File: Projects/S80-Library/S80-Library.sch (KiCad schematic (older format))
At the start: 2 parts, among them U1 ATmega328P-PU

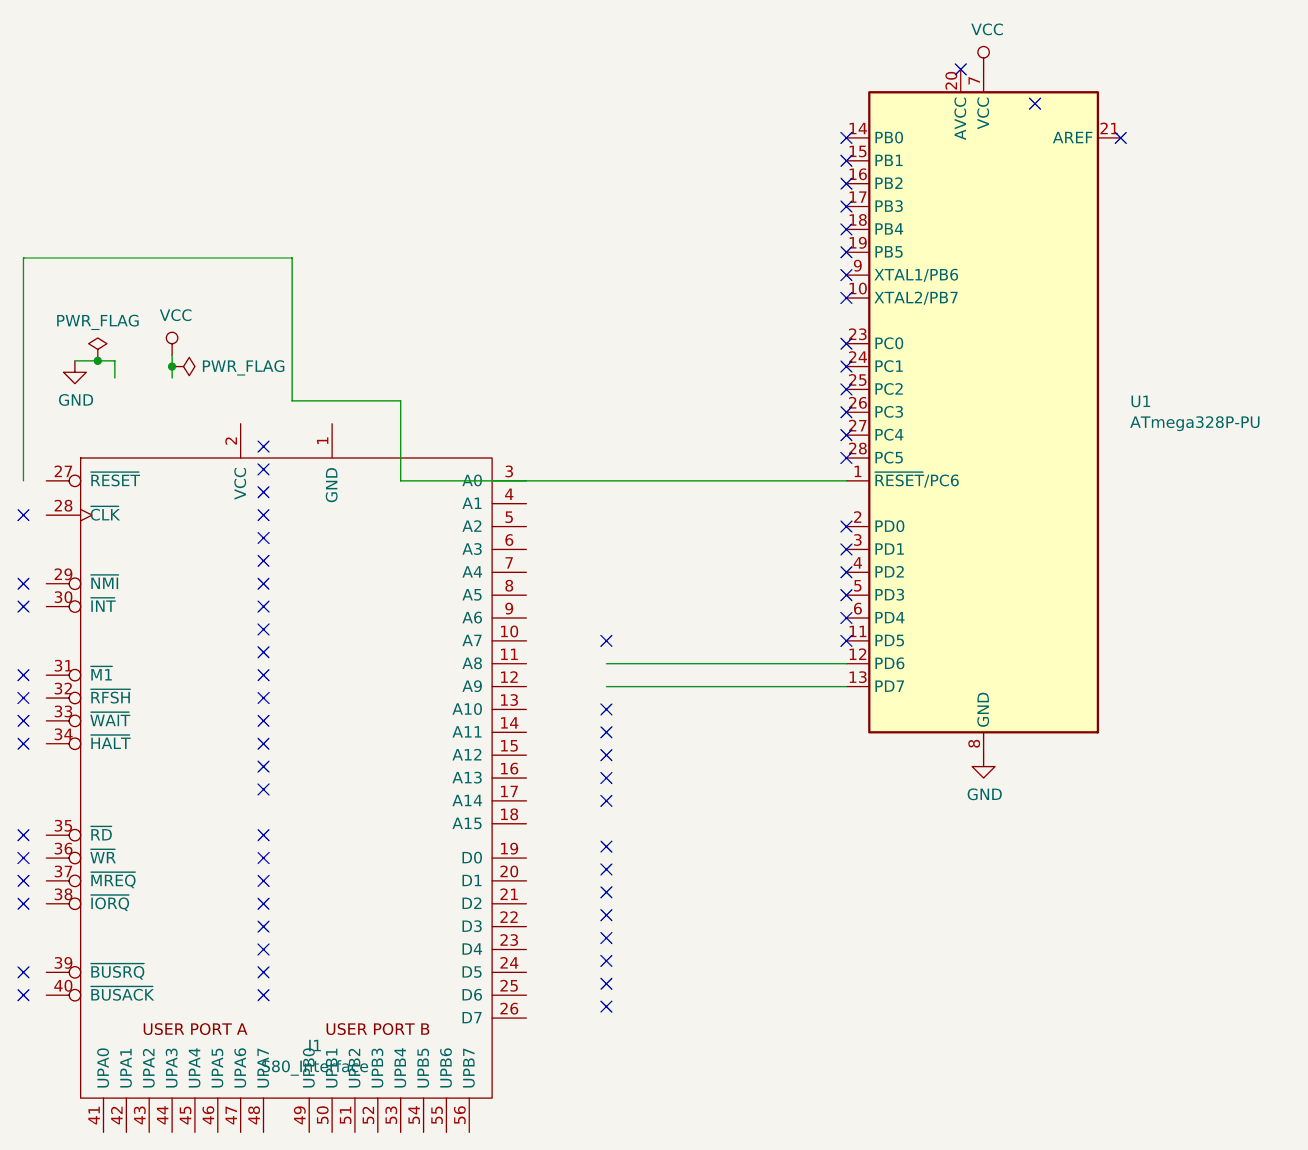
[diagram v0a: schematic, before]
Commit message: added the template
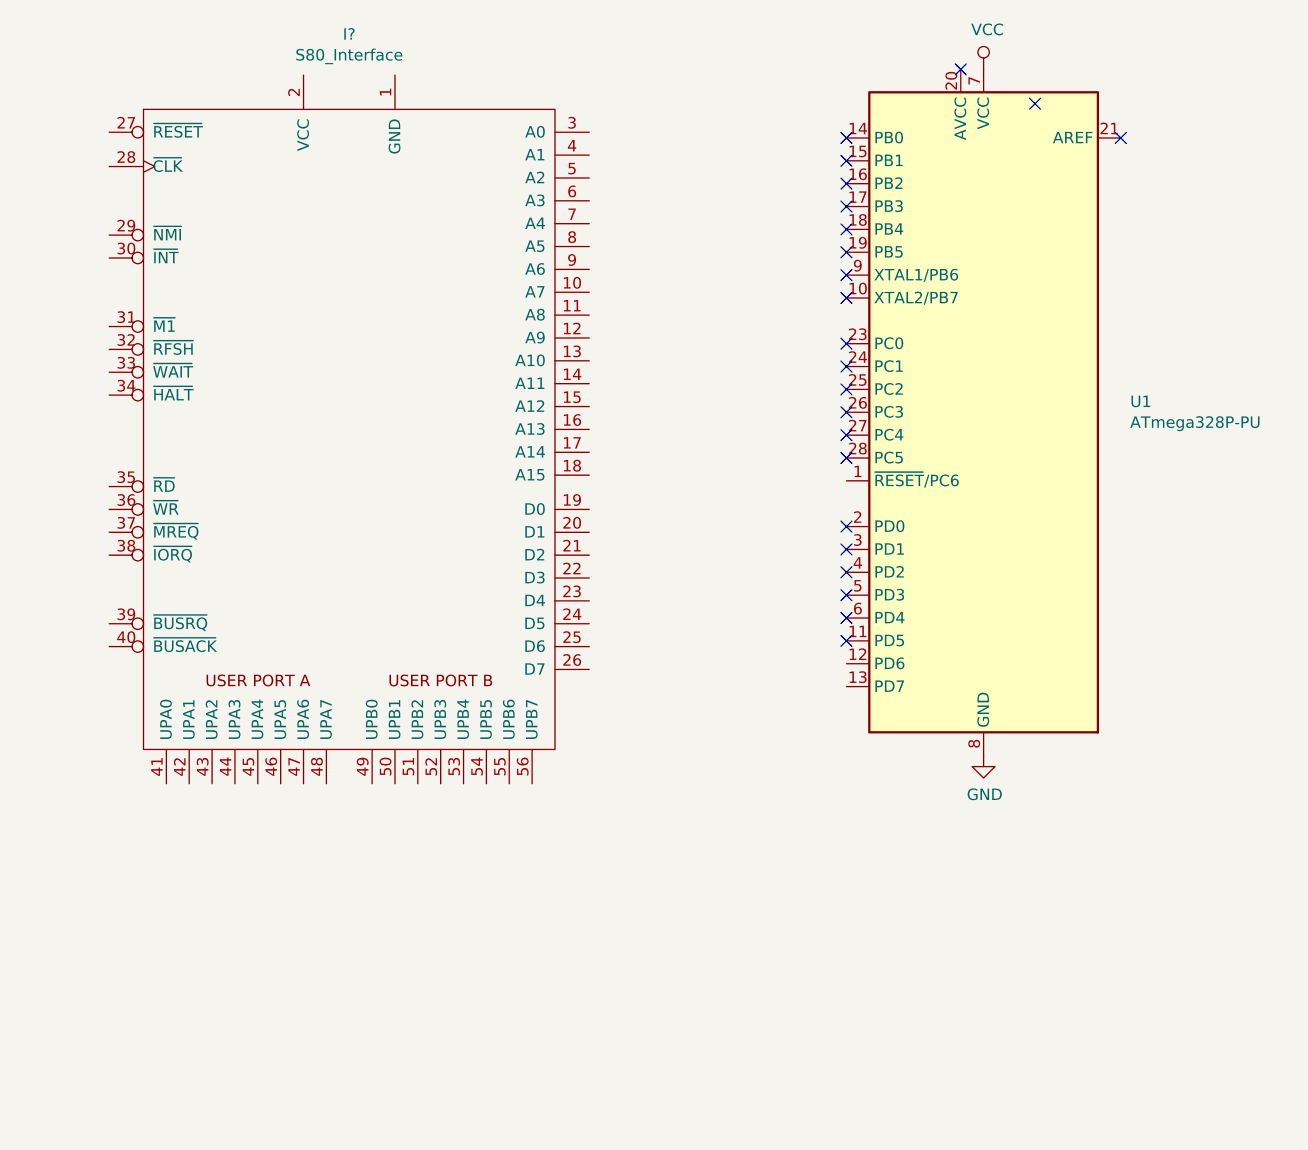
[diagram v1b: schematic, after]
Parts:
- removed I1: S80_Interface, S80:S80-1, symbol S80:S80_Interface
- added I?: S80_Interface, symbol S80:S80_Interface
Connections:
- wire segments 13 -> 0
- no-connect marks 74 -> 23
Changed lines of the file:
@@
 EESchema Schematic File Version 4
+LIBS:S80-Library-cache
 EELAYER 26 0
 EELAYER END
@@
 Comment4 ""
 $EndDescr
-$Comp
-L S80:S80_Interface I1
-U 1 1 5D005A4D
-P 3500 5325
-F 0 "I1" H 3625 4203 50  0000 C CNN
-F 1 "S80_Interface" H 3625 4112 50  0000 C CNN
-F 2 "S80:S80-1" H 2850 6025 50  0001 C CNN
-F 3 "" H 2850 6025 50  0001 C CNN
-	1    3500 5325
-	1    0    0    -1
-$EndComp
 $Comp
 L MCU_Microchip_ATmega:ATmega328P-PU U1
@@
 $EndComp
 $Comp
-L power:GND #PWR0102
-U 1 1 5D005C2C
-P 2575 3450
-F 0 "#PWR0102" H 2575 3200 50  0001 C CNN
-F 1 "GND" H 2580 3277 50  0000 C CNN
-F 2 "" H 2575 3450 50  0001 C CNN
-F 3 "" H 2575 3450 50  0001 C CNN
-	1    2575 3450
-	1    0    0    -1
-$EndComp
-Wire Wire Line
-	2750 3450 2750 3525
-$Comp
 L power:VCC #PWR0103
 U 1 1 5D005CD2
@@
 	1    0    0    -1
 $EndComp
-$Comp
-L power:VCC #PWR0104
-U 1 1 5D005CF8
-P 3000 3425
-F 0 "#PWR0104" H 3000 3275 50  0001 C CNN
-F 1 "VCC" H 3017 3598 50  0000 C CNN
-F 2 "" H 3000 3425 50  0001 C CNN
-F 3 "" H 3000 3425 50  0001 C CNN
-	1    3000 3425
-	1    0    0    -1
-$EndComp
-$Comp
-L power:PWR_FLAG #FLG0101
-U 1 1 5D005F9E
-P 2675 3450
-F 0 "#FLG0101" H 2675 3525 50  0001 C CNN
-F 1 "PWR_FLAG" H 2675 3624 50  0000 C CNN
-F 2 "" H 2675 3450 50  0001 C CNN
-F 3 "~" H 2675 3450 50  0001 C CNN
-	1    2675 3450
-	1    0    0    -1
-$EndComp
-Connection ~ 2675 3450
-Wire Wire Line
-	2675 3450 2750 3450
-Wire Wire Line
-	2575 3450 2675 3450
-$Comp
-L power:PWR_FLAG #FLG0102
-U 1 1 5D006041
-P 3000 3475
-F 0 "#FLG0102" H 3000 3550 50  0001 C CNN
-F 1 "PWR_FLAG" V 3000 3603 50  0000 L CNN
-F 2 "" H 3000 3475 50  0001 C CNN
-F 3 "~" H 3000 3475 50  0001 C CNN
-	1    3000 3475
-	0    1    1    0
-$EndComp
-Wire Wire Line
-	3000 3425 3000 3475
-Connection ~ 3000 3475
-Wire Wire Line
-	3000 3475 3000 3525
 NoConn ~ 6775 2325
-Wire Wire Line
-	4900 4775 5950 4775
-Wire Wire Line
-	4900 4875 5950 4875
-NoConn ~ 3400 4425
-NoConn ~ 3400 4525
-NoConn ~ 3400 4625
-NoConn ~ 3400 4725
-NoConn ~ 3400 4825
-NoConn ~ 3400 4925
-NoConn ~ 3400 5025
-NoConn ~ 3400 5125
-NoConn ~ 3400 5225
-NoConn ~ 3400 5325
-NoConn ~ 4900 4675
-Wire Wire Line
-	2350 3975 2350 3000
-Wire Wire Line
-	2350 3000 3525 3000
-Wire Wire Line
-	3525 3000 3525 3625
-Wire Wire Line
-	3525 3625 4000 3625
-Wire Wire Line
-	4000 3625 4000 3975
-Wire Wire Line
-	4000 3975 5950 3975
-NoConn ~ 2350 4125
-NoConn ~ 2350 4425
-NoConn ~ 2350 4525
-NoConn ~ 2350 4825
-NoConn ~ 2350 4925
-NoConn ~ 2350 5025
-NoConn ~ 2350 5125
-NoConn ~ 2350 5525
-NoConn ~ 2350 5625
-NoConn ~ 2350 5725
-NoConn ~ 2350 5825
-NoConn ~ 2350 6125
-NoConn ~ 2350 6225
-NoConn ~ 3400 4325
-NoConn ~ 3400 4225
-NoConn ~ 3400 4125
-NoConn ~ 3400 4025
-NoConn ~ 3400 3925
-NoConn ~ 3400 3825
-NoConn ~ 3400 5525
-NoConn ~ 3400 5625
-NoConn ~ 3400 5725
-NoConn ~ 3400 5825
-NoConn ~ 3400 5925
-NoConn ~ 3400 6025
-NoConn ~ 3400 6125
-NoConn ~ 3400 6225
-NoConn ~ 4900 4975
-NoConn ~ 4900 5075
-NoConn ~ 4900 5175
-NoConn ~ 4900 5275
-NoConn ~ 4900 5375
-NoConn ~ 4900 5575
-NoConn ~ 4900 5675
-NoConn ~ 4900 5775
-NoConn ~ 4900 5875
-NoConn ~ 4900 5975
-NoConn ~ 4900 6075
-NoConn ~ 4900 6175
-NoConn ~ 4900 6275
 NoConn ~ 5950 2475
 NoConn ~ 5950 2575
@@
 NoConn ~ 5950 4675
 NoConn ~ 6450 2175
+$Comp
+L S80:S80_Interface I?
+U 1 1 5D12C240
+P 3775 3800
+F 0 "I?" H 3775 5578 50  0000 C CNN
+F 1 "S80_Interface" H 3775 5487 50  0000 C CNN
+F 2 "" H 2875 4200 50  0001 C CNN
+F 3 "" H 2875 4200 50  0001 C CNN
+	1    3775 3800
+	1    0    0    -1
+$EndComp
 $EndSCHEMATC
